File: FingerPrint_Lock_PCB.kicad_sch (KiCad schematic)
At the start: 16 parts, among them J1 Arduino_Digital1, J2 Arduino_Digital2, J3 Arduino_Analog, J4 Arduino_Power, J5 Sensor, J6 Relay, J7 LCD, SW1 SW_Push_Dual, SW2 SW_Push_Dual, SW3 SW_Push_Dual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

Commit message: Post-design-review revisions
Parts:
- removed SW1, SW2, SW3, SW4: SW_Push_Dual, Button_Switch_THT:SW_PUSH_6mm_H9.5mm, symbol Switch:SW_Push_Dual
- added J10: Sensor, Connector_PinSocket_2.54mm:PinSocket_1x04_P2.54mm_Vertical, symbol Connector_Generic:Conn_01x04
- added J8: Relay, Connector_PinSocket_2.54mm:PinSocket_1x02_P2.54mm_Vertical, symbol Connector_Generic:Conn_01x02
- added J9: LCD, Connector_PinSocket_2.54mm:PinSocket_1x04_P2.54mm_Vertical, symbol Connector_Generic:Conn_01x04
- added SW1, SW2, SW3, SW4: SW_Push, Button_Switch_THT:SW_PUSH_6mm_H9.5mm, symbol Switch:SW_Push
- added U1: LCD1602-CN0295, Display:RC1602A, symbol Display_Character:RC1602A-GHW-ESX
- added U2: AEDIKO 14921, Relay_THT:Relay_StandexMeder_DIP_LowProfile, symbol Relay:DIPxx-1Cxx-51x
- added U3: ROB-15324, symbol Custom_Syms:ROB-15324
- added U4: JM-101, symbol Custom_Syms:JM-101
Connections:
- net 3V3: now also J10.1 (Pin_1), U4.1 (VCC)
- net 5V: now also J9.1 (Pin_1), U1.2 (VCC)
- net A4_SDA: now also J9.3 (Pin_3), U1.3 (SDA)
- net A5_SCL: now also J9.4 (Pin_4), U1.4 (SCL)
- net D2_RX: now also J10.3 (Pin_3), U4.3 (RX)
- net D3_TX: now also J10.2 (Pin_2), U4.2 (TX)
- net D4: now also SW1.1
- net D5: now also SW2.1
- net D6: now also SW3.1
- net D7: now also SW4.1
- net GND: now also J10.4 (Pin_4), J8.1 (Pin_1), J9.2 (Pin_2), SW1.2, SW2.2, SW3.2, SW4.2, U1.1 (GND), U2.2, U3.2 (-), U4.4 (GND)
- net RELAY_IN: now also J8.2 (Pin_2), U2.3
- net A0: no longer names the net of J3.1 (Pin_1)
- net A1: no longer names the net of J3.2 (Pin_2)
- net A2: no longer names the net of J3.3 (Pin_3)
- net A3: no longer names the net of J3.4 (Pin_4)
- net AREF: no longer names the net of J2.3 (Pin_3)
- net D0: no longer names the net of J1.8 (Pin_8)
- net D1: no longer names the net of J1.7 (Pin_7)
- net D10: no longer names the net of J2.8 (Pin_8)
- net D11: no longer names the net of J2.7 (Pin_7)
- net D12: no longer names the net of J2.6 (Pin_6)
- net D13: no longer names the net of J2.5 (Pin_5)
- net D9: no longer names the net of J2.9 (Pin_9)
- net IOREF: no longer names the net of J4.2 (Pin_2)
- net RESET: no longer names the net of J4.3 (Pin_3)
- net UL1: no longer names the net of J2.2 (Pin_2)
- net UL2: no longer names the net of J2.1 (Pin_1)
- net UL3: no longer names the net of J4.1 (Pin_1)
- net VIN renamed +12V
- net +12V: now also U2.1, U2.5
- new net: U2.4, U3.1 (+)
- no-connect marks 18 -> 22
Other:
- note added: "ARDUINO UNO R3"
- note added: "FINGERPRINT SENSOR"
- note added: "LCD MODULE"
- note added: "PCB ASSEMBLY"
- note added: "RELAY"
- note added: "SOLENOID LATCH"
- note added: "Supply Transformer"
- note added: "To Fingerprint Sensor"
- note added: "To LCD Module"
- note added: "To Relay"
- note added: "UI/NAVIGATION BUTTONS"
- note removed: "Fingerprint Sensor"
- note removed: "LCD Module"
- note removed: "Relay"
- moved on the sheet: J1, J2, J3, J4, J5, J6, J7, R1, R2, R3, R4, R5

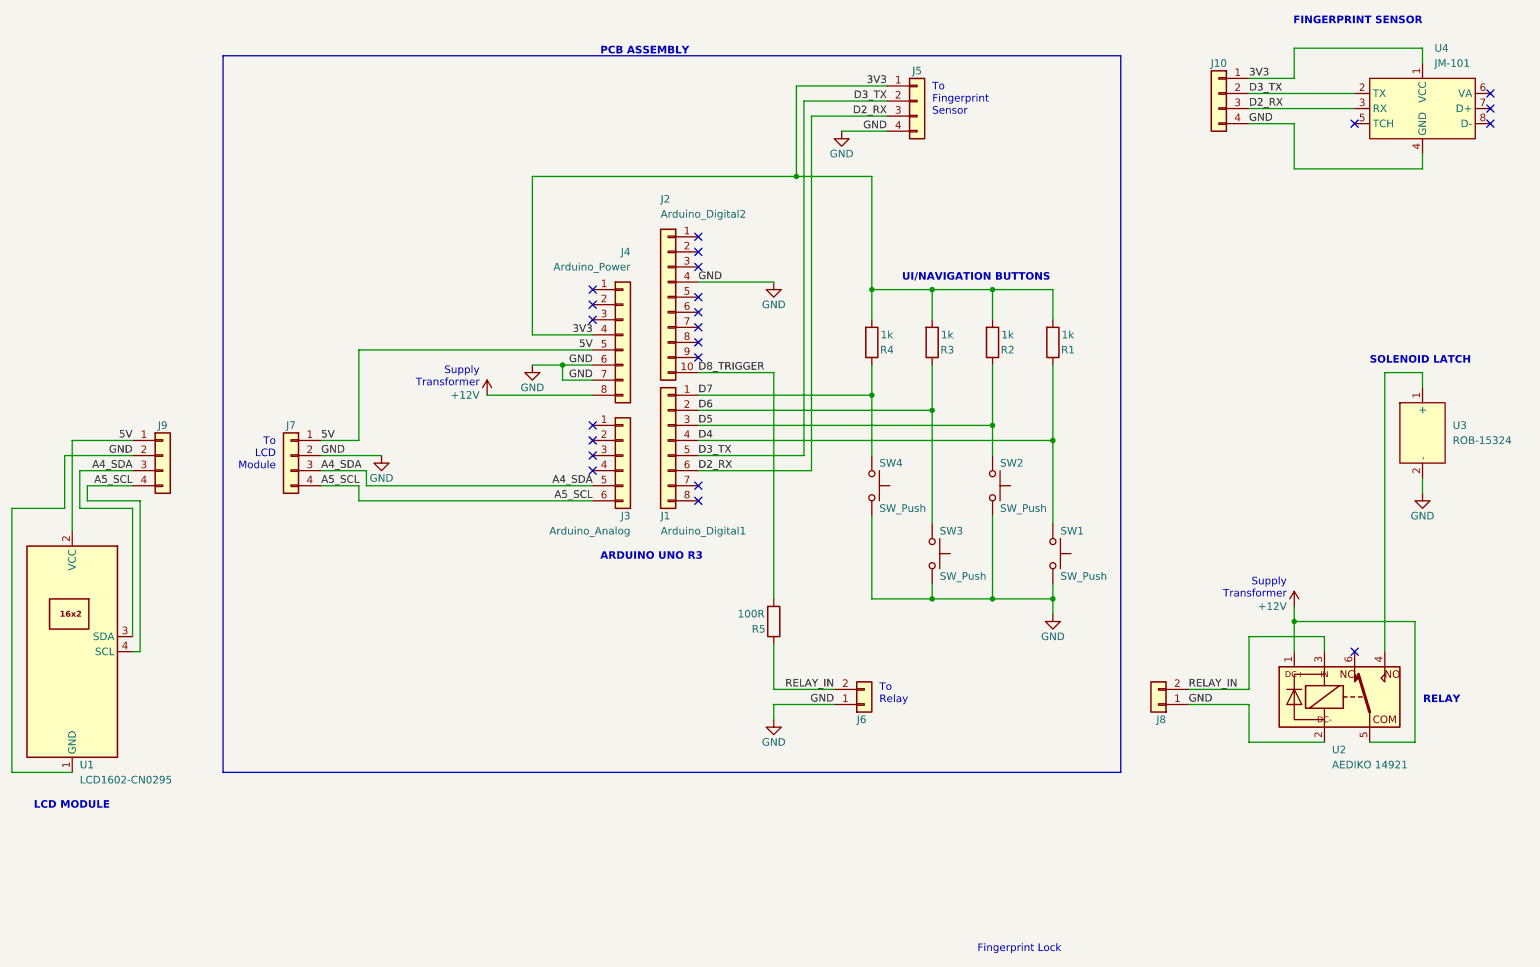
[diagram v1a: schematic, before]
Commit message: Minor changes; updated silkscreen
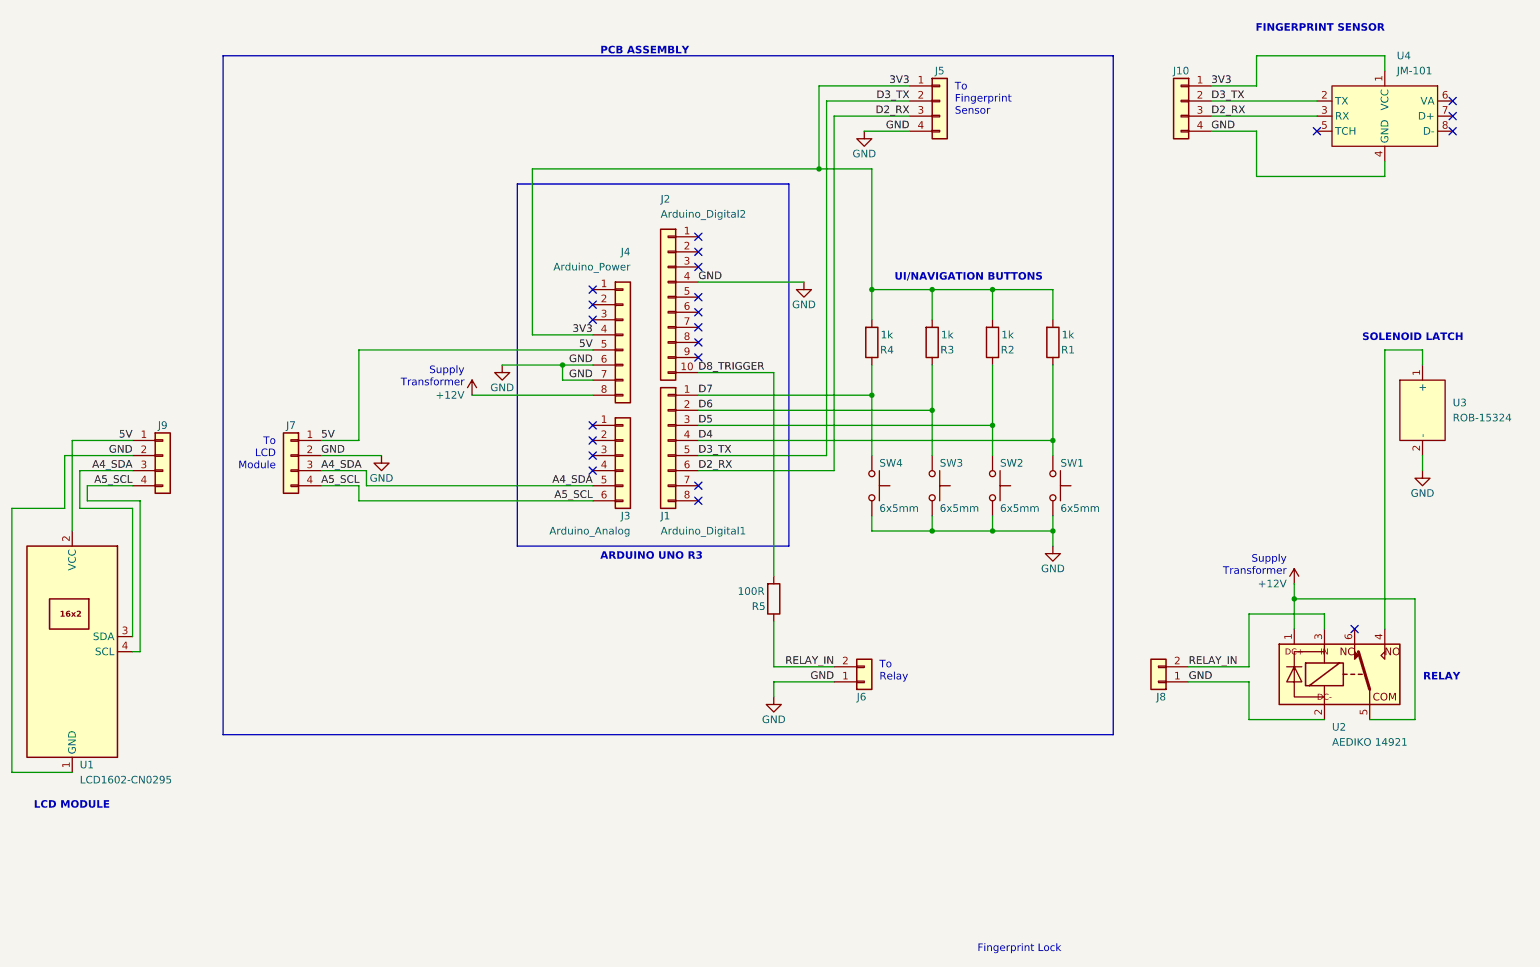
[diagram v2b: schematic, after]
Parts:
- J5, J7: footprint Connector_PinSocket_2.54mm:PinSocket_1x04_P2.54mm_Vertical -> Connector_PinHeader_2.54mm:PinHeader_1x04_P2.54mm_Vertical
- J6: footprint Connector_PinSocket_2.54mm:PinSocket_1x02_P2.54mm_Vertical -> Connector_PinHeader_2.54mm:PinHeader_1x02_P2.54mm_Vertical
- SW1, SW2, SW3, SW4: value SW_Push -> 6x5mm; footprint Button_Switch_THT:SW_PUSH_6mm_H9.5mm -> Button_Switch_THT:SW_PUSH_6mm_H5mm
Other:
- moved on the sheet: J10, J5, J6, J8, R5, SW1, SW3, U2, U3, U4
